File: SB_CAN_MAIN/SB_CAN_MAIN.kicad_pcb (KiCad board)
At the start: 4 copper layers, 53 x 40 mm, 91 parts, among them J1 XT30PB_IN, J2 USB_C_Receptacle_USB2.0_16P, J3 Excluder, J4 PT100, J5 Hotend, J6 FAN2, J7 LDC, J8 FS, J9 FAN, Q1 BUK9M8R5-40EX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

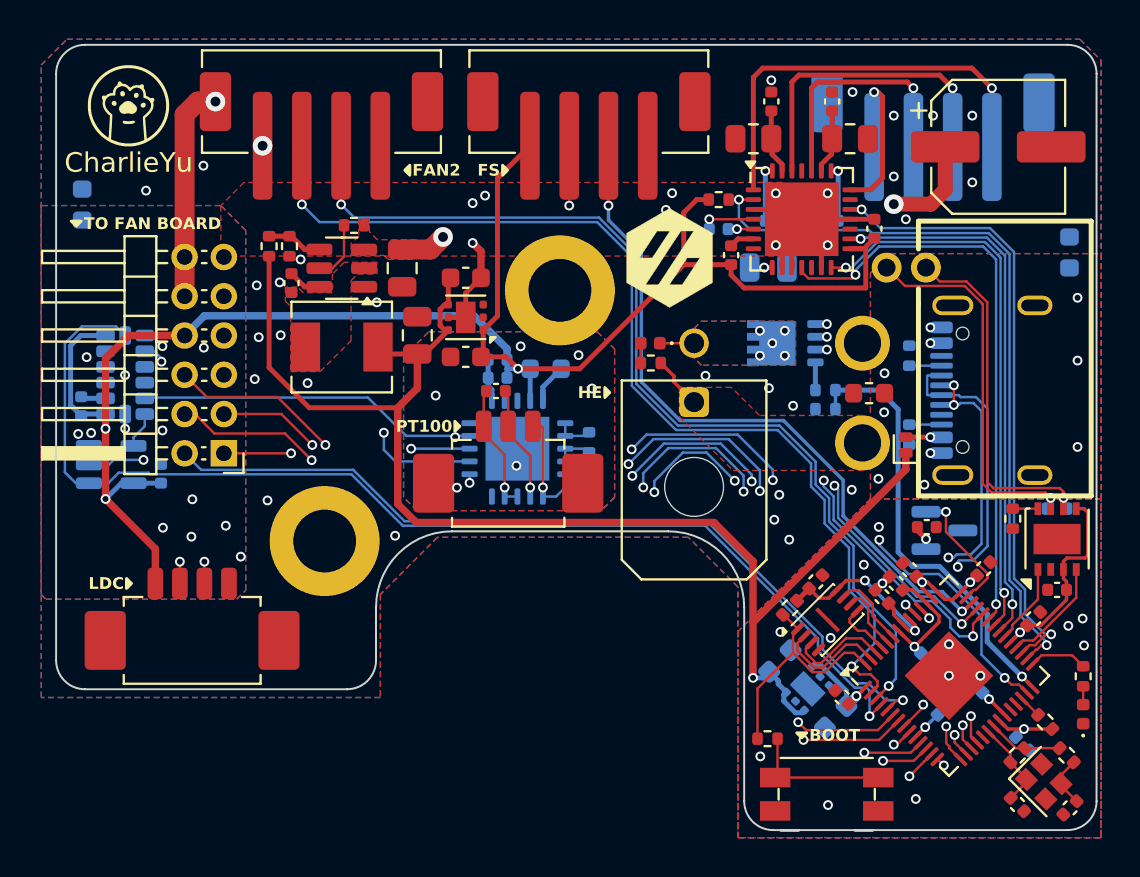
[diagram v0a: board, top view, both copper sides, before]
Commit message: layout: add fan board
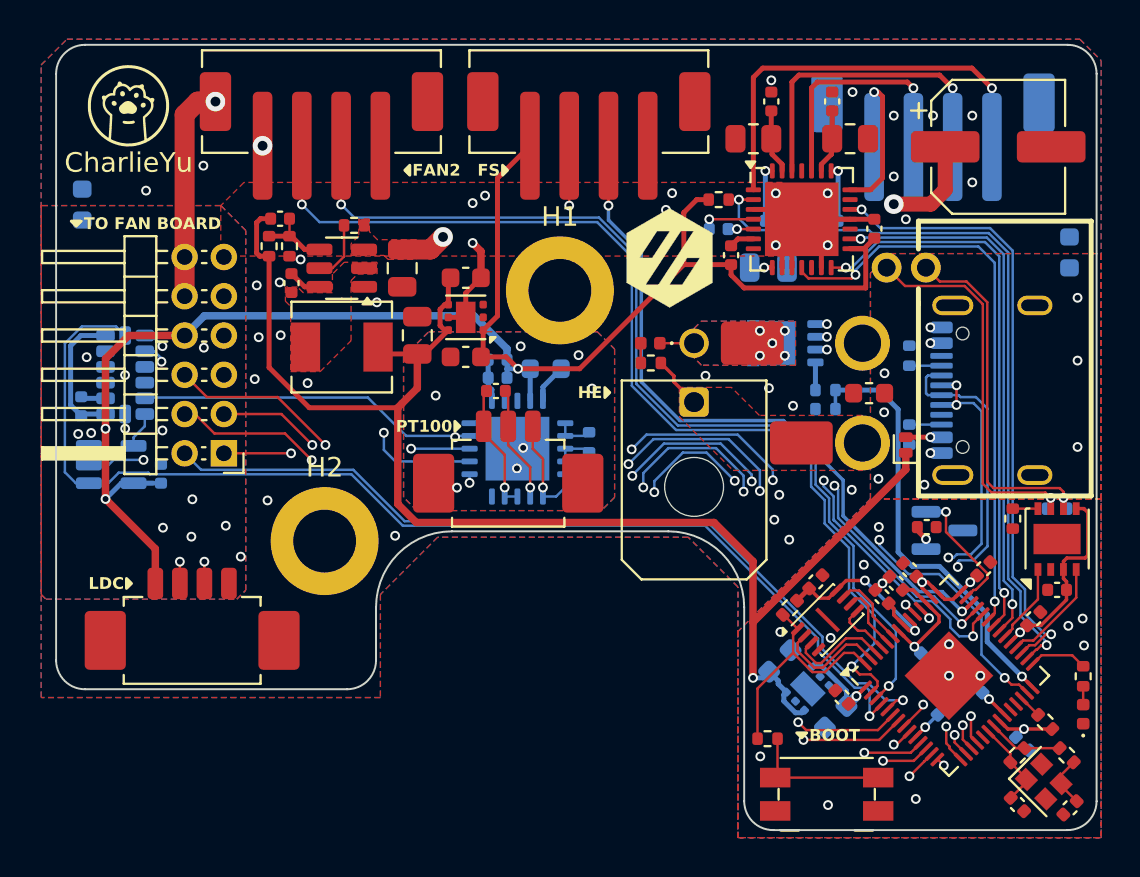
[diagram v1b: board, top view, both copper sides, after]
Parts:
- added C37: 47pF, Capacitor_SMD:C_0402_1005Metric, F.Cu at (91.0, 102.5)
- added TP1: PAD, Library:PAD, F.Cu at (117.6, 113.9)
- added TP2: PAD, Library:PAD, F.Cu at (115.1, 108.9)
- H1, H2: value MountingHole_Pad -> M3; footprint MountingHole:MountingHole_3.2mm_M3_DIN965_Pad -> MountingHole:MountingHole_3.2mm_M3_ISO14580_Pad
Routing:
- net +5V: track 69.9 -> 73.0 mm
- net Net-(U4-VFB): track 2.74 -> 3.63 mm
- net GND: vias 49 -> 50

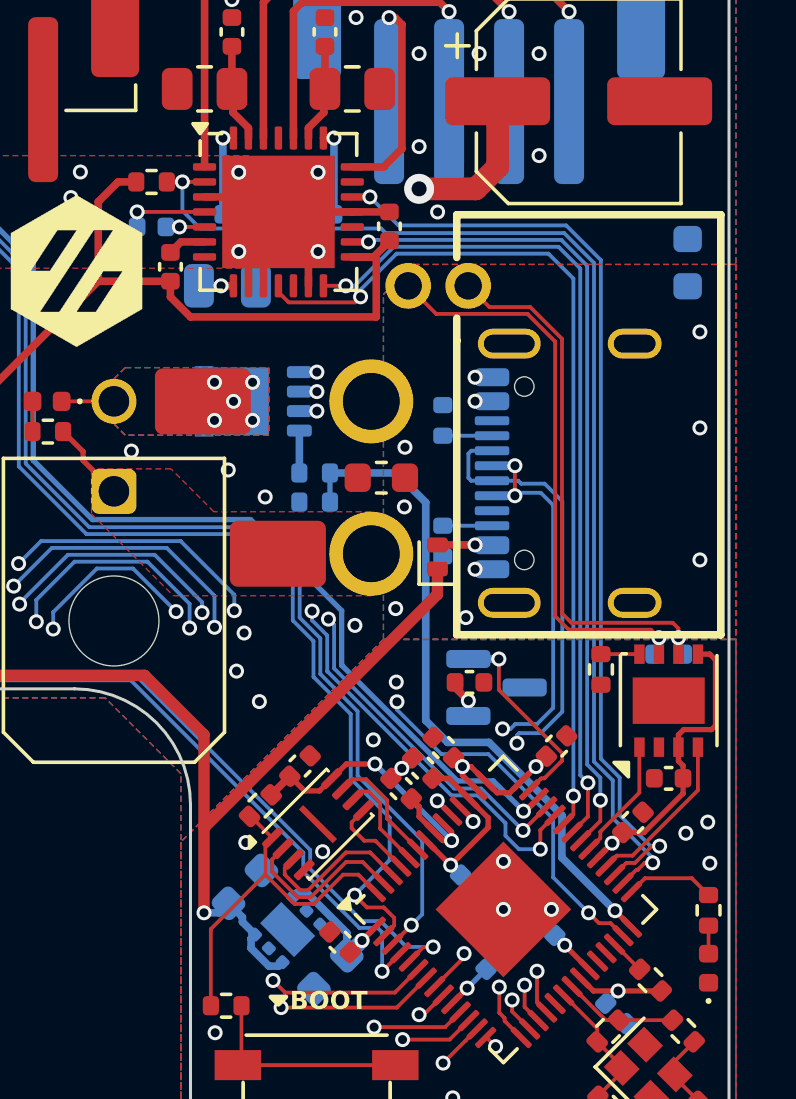
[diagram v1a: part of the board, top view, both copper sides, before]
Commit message: sch: fix bug that the tja1044 can only use 5V power
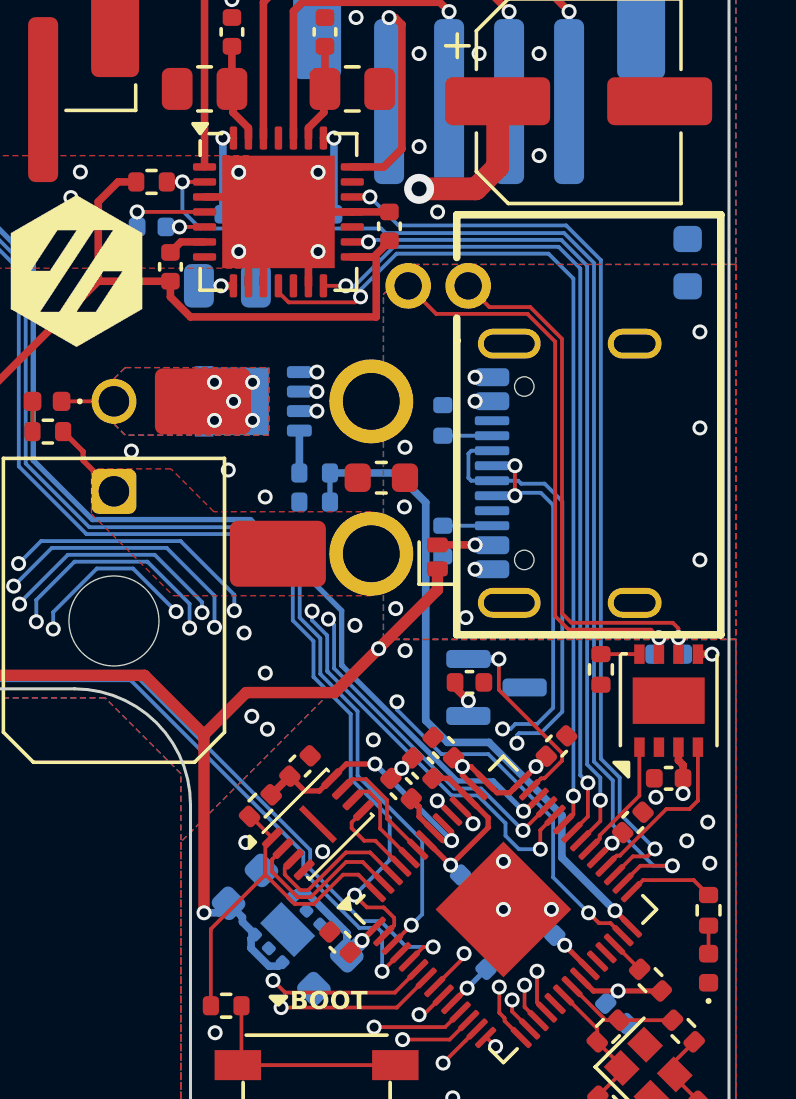
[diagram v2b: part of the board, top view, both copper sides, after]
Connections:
- C14 pad 1: +3V3A -> +5V
- U3 pad 3: +3V3A -> +5V
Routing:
- net +5V: track 73.0 -> 87.1 mm, vias 1 -> 3
- net /TMC_EN: track 38.7 -> 40.1 mm
- net +3V3A: track 43.0 -> 43.4 mm, vias 9 -> 10
- net PGND: vias 31 -> 32
- net GND: vias 50 -> 51
